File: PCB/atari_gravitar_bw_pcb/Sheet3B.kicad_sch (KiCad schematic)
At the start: 0 parts

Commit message: Sheet 3B complete
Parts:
- added C1, C10, C109, C11, C12, C126, C13, C14, C15, C18, C19, C2, C20, C21, C22, C25, C26, C3, C37, C4, C40, C41, C42, C43, C45, C46, C47, C48, C49, C5, C50, C51, C52, C53, C54, C55, C56, C57, C58, C59, C6, C60, C61, C62, C63, C7, C8: .1, symbol Device:C
- added C110: 2.2uf 35V, symbol Device:C_Polarized_US
- added C111, C121: 22uf 25V, symbol Device:C_Polarized_US
- added C117, C119, C120: 100uf 35V, symbol Device:C_Polarized_US
- added C23: 100pf, symbol Device:C
- added C24: 39pf, symbol Device:C
- added CR3: 1N914, symbol Device:D
- added CR5, CR7: 1N100, symbol Device:D
- added CR6: BLUE LED, symbol Device:LED
- added CR8: 1N754A, symbol Device:D_Zener
- added E_4: 74LS193, symbol atari:74LS193
- added E_4: 74LS00, symbol atari:74LS00
- added F_3: 74S04, symbol atari:74LS04
- added F_4, H_4: 74LS393, symbol atari:74LS393
- added F_7: 74LS14, symbol atari:74LS14
- added K_3: 74LS74, symbol atari:74LS74
- added L1: 100uh, symbol Device:L
- added L_4: 74LS08, symbol atari:74LS08
- added Q1: 2N3904, Package_TO_SOT_THT:TO-92_Inline, symbol Transistor_BJT:2N3904
- added R107, R23, R55, R71, R82: 1k, symbol Device:R_US
- added R195: 270 1/2W, symbol Device:R_US
- added R22, R40, R41, R72: 10k, symbol Device:R_US
- added R42, R73: 220, symbol Device:R_US
- added R69: 22k, symbol Device:R_US
- added R70: 68k, symbol Device:R_US
- added R_8: TL082, symbol atari:TL082
- added TP-15V1, TP12MHZ1, TP15V1, TP5V1, TP5V2, TP6.8V1, TP6MHZ1, TPGND1, TPGND2, TPGND3, TPGND4, TPGND5, TPGND6, TPPHI01, TPRESET1, TP~{RESET}1: tp_2_pin, symbol atari:tp_2_pin
- added VR1: L7915, symbol atari:L7915
- added VR2: L7815, symbol atari:L7815
- added Y1: 12.096MHz, symbol Device:Crystal
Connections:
- new net: C23.1, Q1.2 (B), R40.1, R41.2, Y1.2
- new net: R70.2, R71.1, R73.1, R_8.1
- new net: R69.2, R70.1, R72.2, R_8.3 (+)
- new net: CR6.2 (A), R107.2
- new net: C23.2, C24.1, F_3.11, L1.1, Q1.1 (E)
- new net: L1.2, R42.1
- new net: K_3.2 (D), L_4.8
- new net: CR3.2 (A), F_7.3, R71.2, TPRESET1.1, TPRESET1.2
- new net: H_4.6 (1QD), K_3.3 (C)
- new net: E_4.7 (QD), F_4.13 (2CK)
- new net: E_4.3, H_4.12 (2CLR), H_4.2 (1CLR)
- new net: H_4.1 (1CK), H_4.8 (2QD)
- new net: F_4.1 (1CK), F_4.8 (2QD)
- new net +10V: C55.1, R72.1, R_8.8 (V+)
- new net +15V: C121.1, CR7.1 (K), R195.1, TP15V1.1, TP15V1.2, VR2.3 (OUT)
- new net +24V: C120.1, VR2.1 (IN)
- new net +5V: C1.1, C10.1, C109.1, C11.1, C117.1, C12.1, C13.1, C14.1, C15.1, C18.1, C19.1, C2.1, C20.1, C21.1, C22.2, C25.1, C26.1, C3.1, C37.1, C4.1, C40.1, C41.1, C42.1, C43.1, C45.1, C46.1, C47.1, C48.1, C49.1, C5.1, C50.1, C51.1, C52.1, C53.1, C54.1, C56.1, C57.1, C58.1, C59.1, C6.1, C60.1, C61.1, C62.1, C63.1, C7.1, C8.1, CR3.1 (K), E_4.16 (VCC), F_4.14 (VCC), H_4.14 (VCC), K_3.14 (VCC), Q1.3 (C), R107.1, R22.1, R23.2, R41.1, R55.2, R82.2, R_8.2 (-), TP5V1.1, TP5V1.2, TP5V2.1, TP5V2.2
- new net +6V: C126.1, CR8.1 (K), R195.2, TP6.8V1.1, TP6.8V1.2
- new net -15V: C111.2, CR5.2 (A), TP-15V1.1, TP-15V1.2, VR1.3 (VO)
- new net -24V: C110.2, C119.2, VR1.2 (VI)
- new net 1.5MHZ: E_4.6 (QC), TPPHI01.1, TPPHI01.2
- new net 12KHZ: F_4.4 (1QB)
- new net 12MHZ: E_4.5 (D2), F_3.10, TP12MHZ1.1, TP12MHZ1.2
- new net 3KHZ: F_4.6 (1QD), H_4.13 (2CK)
- new net 3MHZ: E_4.2 (QB)
- new net 6MHZ: E_4.3 (QA), TP6MHZ1.1, TP6MHZ1.2
- new net GND: C1.2, C10.2, C109.2, C11.2, C110.1, C111.1, C117.2, C119.1, C12.2, C120.2, C121.2, C126.2, C13.2, C14.2, C15.2, C18.2, C19.2, C2.2, C20.2, C21.2, C22.1, C24.2, C25.2, C26.2, C3.2, C37.2, C4.2, C40.2, C41.2, C42.2, C43.2, C45.2, C46.2, C47.2, C48.2, C49.2, C5.2, C50.2, C51.2, C52.2, C53.2, C54.2, C55.2, C56.2, C57.2, C58.2, C59.2, C6.2, C60.2, C61.2, C62.2, C63.2, C7.2, C8.2, CR5.1 (K), CR6.1 (K), CR7.2 (A), CR8.2 (A), E_4.8 (GND), F_4.7 (GND), H_4.7 (GND), K_3.7 (GND), L_4.10, R40.2, R42.2, R69.1, R73.2, R_8.4 (V-), TPGND1.1, TPGND1.2, TPGND2.1, TPGND2.2, TPGND3.1, TPGND3.2, TPGND4.1, TPGND4.2, TPGND5.1, TPGND5.2, TPGND6.1, TPGND6.2, TP~{RESET}1.1, TP~{RESET}1.2, VR1.1 (GND), VR2.2 (GND), Y1.1
- new net POR: E_4.14 (C), F_4.12 (2CLR), F_4.2 (1CLR), F_7.4, F_7.5
- new net PR23: E_4.1 (B), E_4.10 (C), E_4.11 (LD), E_4.15 (A), E_4.4 (D1), E_4.9 (D), K_3.1 (~{R}), R23.1
- new net PR55: R55.1
- new net PR82: R82.1
- new net ~{POR}: E_4.2, F_7.6, K_3.4 (~{S})
- new net ~{RESET}: K_3.6 (~{Q})
- new net ~{WDCLR}: E_4.1
- new net ~{WDDIS}: L_4.9, R22.2
- no-connect marks 0 -> 8
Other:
- note added: "CLOCK"
- note added: "POWER INPUT"
- note added: "POWER-ON RESET"
- note added: "WATCHDOG"

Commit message: Worked on the schematic library
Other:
- moved on the sheet: C1, C10, C109, C11, C110, C111, C117, C119, C12, C120, C121, C126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

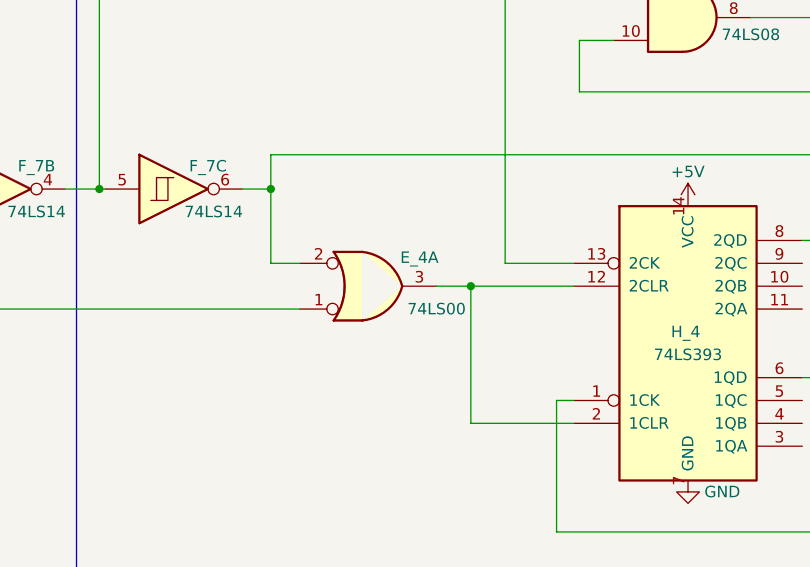
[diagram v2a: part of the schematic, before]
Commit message: Completed sheet 4b
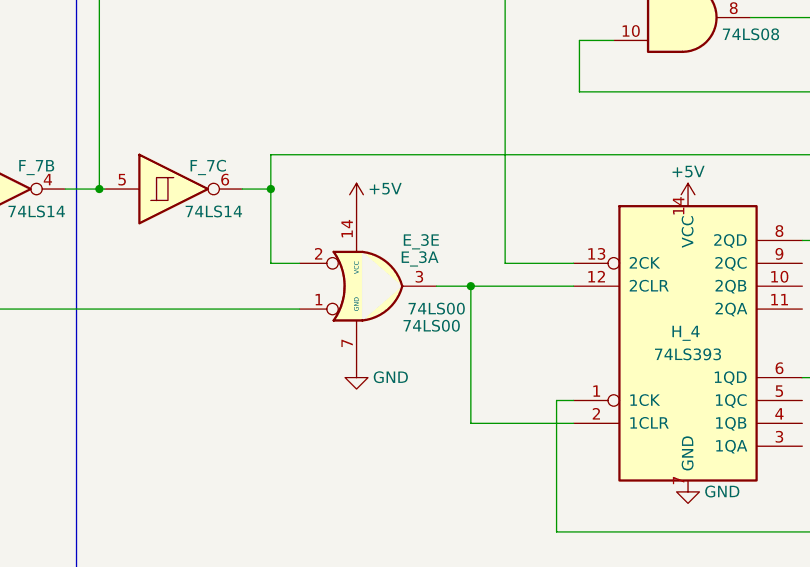
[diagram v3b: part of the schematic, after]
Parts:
- added unit 5 of E_3
- renumbered E_4 to E_3
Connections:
- net +5V: now also E_3.14 (VCC)
- net GND: now also E_3.7 (GND)
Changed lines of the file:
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@@
+    (pin "1")
+  )
+  (symbol (lib_id "power:GND") (at 271.78 193.04 0) (unit 1)
+    (in_bom yes) (on_board yes)
+    (property "Reference" "#PWR0196" (id 0) (at 271.78 199.39 0)
+      (effects (font (size 1.27 1.27)) hide)
+    )
+    (property "Value" "GND" (id 1) (at 275.59 194.31 0))
+    (property "Footprint" "" (id 2) (at 271.78 193.04 0)
+      (effects (font (size 1.27 1.27)) hide)
+    )
+    (property "Datasheet" "" (id 3) (at 271.78 193.04 0)
+      (effects (font (size 1.27 1.27)) hide)
+    )
     (pin "1")
   )
@@
     (pin "1")
     (pin "2")
+  )
+  (symbol (lib_id "power:+5V") (at 271.78 175.26 0) (unit 1)
+    (in_bom yes) (on_board yes)
+    (property "Reference" "#PWR0197" (id 0) (at 271.78 179.07 0)
+      (effects (font (size 1.27 1.27)) hide)
+    )
+    (property "Value" "+5V" (id 1) (at 273.05 173.355 0)
+      (effects (font (size 1.27 1.27)) (justify left))
+    )
+    (property "Footprint" "" (id 2) (at 271.78 175.26 0)
+      (effects (font (size 1.27 1.27)) hide)
+    )
+    (property "Datasheet" "" (id 3) (at 271.78 175.26 0)
+      (effects (font (size 1.27 1.27)) hide)
+    )
+    (pin "1")
   )
   (symbol (lib_id "Device:C") (at 109.855 174.625 0) (unit 1)
@@
     )
     (property "Datasheet" "" (id 3) (at 345.44 194.31 0)
+      (effects (font (size 1.27 1.27)) hide)
+    )
+    (pin "14")
+    (pin "7")
+  )
+  (symbol (lib_id "atari:74LS00") (at 271.78 184.15 0) (unit 5)
+    (in_bom yes) (on_board yes)
+    (property "Reference" "E_3" (id 0) (at 276.86 179.07 0)
+      (effects (font (size 1.27 1.27)) (justify left))
+    )
+    (property "Value" "74LS00" (id 1) (at 276.86 188.595 0)
+      (effects (font (size 1.27 1.27)) (justify left))
+    )
+    (property "Footprint" "" (id 2) (at 271.78 184.15 0)
+      (effects (font (size 1.27 1.27)) hide)
+    )
+    (property "Datasheet" "" (id 3) (at 271.78 184.15 0)
       (effects (font (size 1.27 1.27)) hide)
     )
@@
   (symbol (lib_id "atari:74LS00") (at 273.05 184.15 0) (mirror x) (unit 1) (convert 2)
     (in_bom yes) (on_board yes)
-    (property "Reference" "E_4" (id 0) (at 278.765 180.975 0))
+    (property "Reference" "E_3" (id 0) (at 278.765 180.975 0))
     (property "Value" "74LS00" (id 1) (at 280.67 186.69 0))
     (property "Footprint" "" (id 2) (at 273.05 184.15 0)

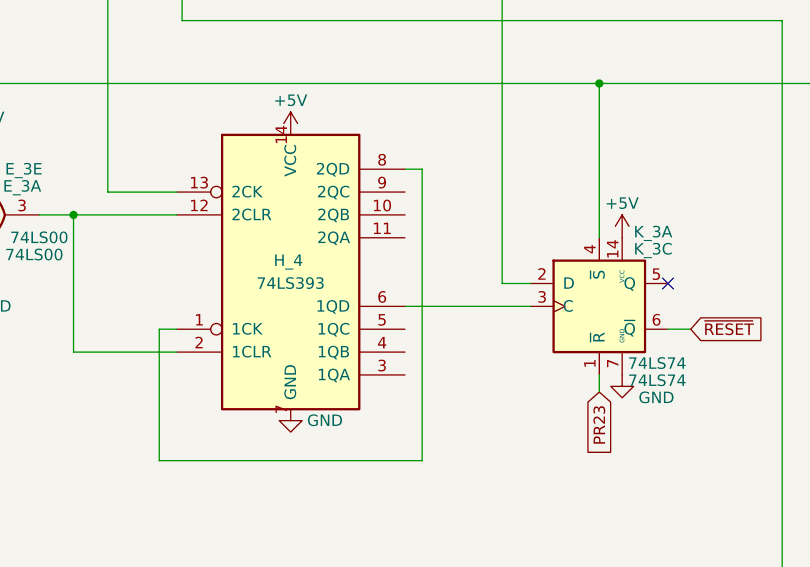
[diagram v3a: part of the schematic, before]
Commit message: Completed sheet 8B
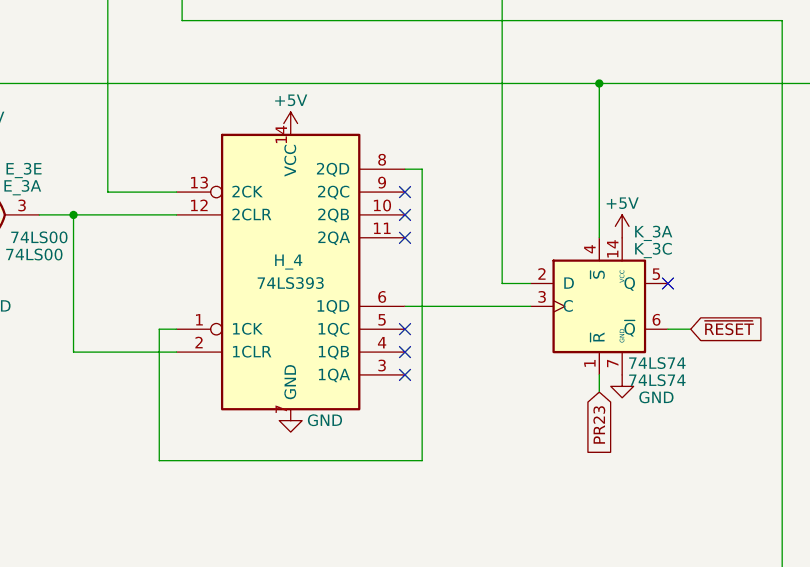
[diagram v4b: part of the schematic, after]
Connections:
- no-connect marks 8 -> 14
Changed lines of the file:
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@@
   (no_connect (at 272.415 44.45))
   (no_connect (at 350.52 191.77))
+  (no_connect (at 321.31 186.69))
+  (no_connect (at 321.31 196.85))
+  (no_connect (at 321.31 199.39))
+  (no_connect (at 321.31 201.93))
+  (no_connect (at 321.31 184.15))
+  (no_connect (at 321.31 181.61))
   (no_connect (at 292.1 83.82))
   (no_connect (at 292.1 86.36))
